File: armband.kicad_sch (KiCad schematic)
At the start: 14 parts, among them IC1 QSMP-1570, SW1 SW_MEC_5G, SW2 SW_MEC_5G

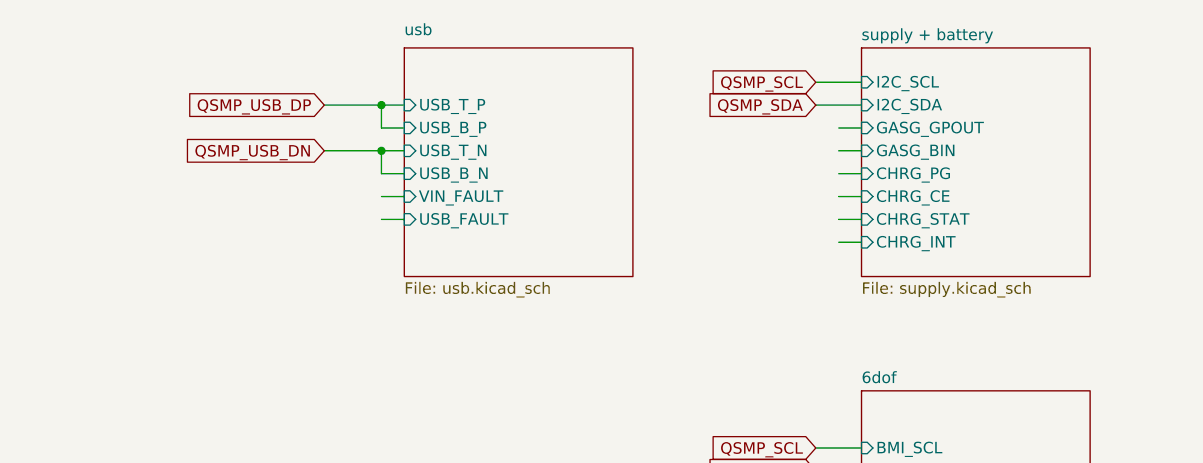
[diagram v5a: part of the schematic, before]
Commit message: switched to other charge + protection IC
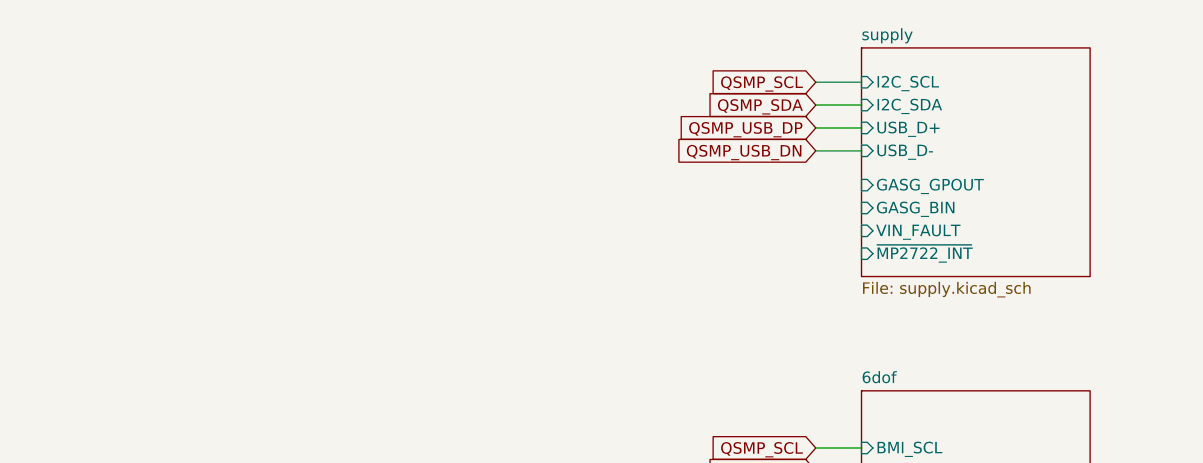
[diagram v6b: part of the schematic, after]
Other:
- sheet supply + battery renamed supply
- removed sheet usb
- sheet supply ports: added USB_D+, USB_D-, VIN_FAULT, ~{MP2722_INT}; removed CHRG_CE, CHRG_INT, CHRG_PG, CHRG_STAT
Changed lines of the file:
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@@
   (junction (at 44.45 99.06) (diameter 0) (color 0 0 0 0)
   )
-  (junction (at 314.96 31.75) (diameter 0) (color 0 0 0 0)
-  )
   (junction (at 35.56 40.64) (diameter 0) (color 0 0 0 0)
   )
@@
   (junction (at 190.5 248.92) (diameter 0) (color 0 0 0 0)
   )
-  (junction (at 314.96 36.83) (diameter 0) (color 0 0 0 0)
-  )
   (junction (at 185.42 55.88) (diameter 0) (color 0 0 0 0)
   )
@@
     (stroke (width 0) (type default))
   )
-  (wire (pts (xy 317.5 39.37) (xy 314.96 39.37))
-    (stroke (width 0) (type default))
-  )
-  (wire (pts (xy 365.76 41.91) (xy 368.3 41.91))
+  (wire (pts (xy 363.22 36.83) (xy 368.3 36.83))
     (stroke (width 0) (type default))
   )
@@
     (stroke (width 0) (type default))
   )
-  (wire (pts (xy 308.61 31.75) (xy 314.96 31.75))
-    (stroke (width 0) (type default))
-  )
   (polyline (pts (xy 25.4 121.92) (xy 25.4 76.2))
     (stroke (width 0) (type default))
@@
     (stroke (width 0) (type default))
   )
-  (wire (pts (xy 314.96 36.83) (xy 317.5 36.83))
-    (stroke (width 0) (type default))
-  )
   (wire (pts (xy 363.22 29.21) (xy 368.3 29.21))
     (stroke (width 0) (type default))
@@
     (stroke (width 0) (type default))
   )
-  (wire (pts (xy 365.76 34.29) (xy 368.3 34.29))
-    (stroke (width 0) (type default))
-  )
   (wire (pts (xy 233.68 213.36) (xy 236.22 213.36))
     (stroke (width 0) (type default))
@@
     (stroke (width 0) (type default))
   )
-  (wire (pts (xy 317.5 34.29) (xy 314.96 34.29))
-    (stroke (width 0) (type default))
-  )
   (wire (pts (xy 48.26 40.64) (xy 53.34 40.64))
     (stroke (width 0) (type default))
   )
-  (wire (pts (xy 308.61 36.83) (xy 314.96 36.83))
-    (stroke (width 0) (type default))
-  )
   (wire (pts (xy 33.02 257.81) (xy 38.1 257.81))
     (stroke (width 0) (type default))
@@
     (stroke (width 0) (type default))
   )
+  (wire (pts (xy 363.22 34.29) (xy 368.3 34.29))
+    (stroke (width 0) (type default))
+  )
   (wire (pts (xy 81.28 93.98) (xy 81.28 96.52))
     (stroke (width 0) (type default))
@@
     (stroke (width 0) (type default))
   )
-  (wire (pts (xy 314.96 36.83) (xy 314.96 39.37))
-    (stroke (width 0) (type default))
-  )
-  (wire (pts (xy 365.76 39.37) (xy 368.3 39.37))
-    (stroke (width 0) (type default))
-  )
   (polyline (pts (xy 25.4 76.2) (xy 101.6 76.2))
     (stroke (width 0) (type default))
@@
     (stroke (width 0) (type default))
   )
-  (wire (pts (xy 314.96 41.91) (xy 317.5 41.91))
-    (stroke (width 0) (type default))
-  )
   (wire (pts (xy 363.22 190.5) (xy 368.3 190.5))
     (stroke (width 0) (type default))
@@
     (stroke (width 0) (type default))
   )
-  (wire (pts (xy 314.96 31.75) (xy 317.5 31.75))
-    (stroke (width 0) (type default))
-  )
   (wire (pts (xy 81.28 257.81) (xy 83.82 257.81))
     (stroke (width 0) (type default))
@@
     (stroke (width 0) (type default))
   )
-  (wire (pts (xy 365.76 36.83) (xy 368.3 36.83))
-    (stroke (width 0) (type default))
-  )
   (wire (pts (xy 41.91 99.06) (xy 44.45 99.06))
     (stroke (width 0) (type default))
@@
     (stroke (width 0) (type default))
   )
-  (wire (pts (xy 314.96 44.45) (xy 317.5 44.45))
-    (stroke (width 0) (type default))
-  )
   (wire (pts (xy 185.42 55.88) (xy 187.96 55.88))
     (stroke (width 0) (type default))
@@
     (stroke (width 0) (type default))
   )
-  (wire (pts (xy 314.96 31.75) (xy 314.96 34.29))
-    (stroke (width 0) (type default))
-  )
   (wire (pts (xy 190.5 50.8) (xy 190.5 53.34))
     (stroke (width 0) (type default))
@@
     (stroke (width 0) (type default))
   )
-  (wire (pts (xy 365.76 46.99) (xy 368.3 46.99))
-    (stroke (width 0) (type default))
-  )
   (wire (pts (xy 81.28 96.52) (xy 83.82 96.52))
     (stroke (width 0) (type default))
@@
   )
   (wire (pts (xy 81.28 86.36) (xy 81.28 88.9))
-    (stroke (width 0) (type default))
-  )
-  (wire (pts (xy 365.76 44.45) (xy 368.3 44.45))
     (stroke (width 0) (type default))
   )
@@
     )
   )
-  (global_label "QSMP_USB_DN" (shape input) (at 308.61 36.83 180) (fields_autoplaced)
-    (effects (font (size 1.27 1.27)) (justify right))
-    (property "Intersheetrefs" "${INTERSHEET_REFS}" (at 292.0971 36.83 0)
+  (global_label "QSMP_USB_DN" (shape input) (at 363.22 36.83 180) (fields_autoplaced)
+    (effects (font (size 1.27 1.27)) (justify right))
+    (property "Intersheetrefs" "${INTERSHEET_REFS}" (at 346.7071 36.83 0)
       (effects (font (size 1.27 1.27)) (justify right) hide)
     )
@@
     )
   )
-  (global_label "QSMP_USB_DP" (shape input) (at 308.61 31.75 180) (fields_autoplaced)
-    (effects (font (size 1.27 1.27)) (justify right))
-    (property "Intersheetrefs" "${INTERSHEET_REFS}" (at 292.1576 31.75 0)
+  (global_label "QSMP_USB_DP" (shape input) (at 363.22 34.29 180) (fields_autoplaced)
+    (effects (font (size 1.27 1.27)) (justify right))
+    (property "Intersheetrefs" "${INTERSHEET_REFS}" (at 346.7676 34.29 0)
       (effects (font (size 1.27 1.27)) (justify right) hide)
     )
@@
         (path "/017c50c6-333c-4d31-ad5a-278994a09b14/ae5dc462-dca9-40e4-ba02-6b87a86a4904"
           (reference "C14") (unit 1)
-        )
-        (path "/017c50c6-333c-4d31-ad5a-278994a09b14/1029a9a3-b5d0-4240-805b-4fc2e9ca6858"
-          (reference "C19") (unit 1)
         )
       )
@@
         (path "/017c50c6-333c-4d31-ad5a-278994a09b14/ae5dc462-dca9-40e4-ba02-6b87a86a4904"
           (reference "C14") (unit 1)
-        )
-        (path "/017c50c6-333c-4d31-ad5a-278994a09b14/1029a9a3-b5d0-4240-805b-4fc2e9ca6858"
-          (reference "C19") (unit 1)
         )
       )
@@
           (reference "#PWR028") (unit 1)
         )
-        (path "/017c50c6-333c-4d31-ad5a-278994a09b14/1029a9a3-b5d0-4240-805b-4fc2e9ca6858"
-          (reference "#PWR011") (unit 1)
-        )
       )
     )
@@
           (reference "#PWR022") (unit 1)
         )
-        (path "/017c50c6-333c-4d31-ad5a-278994a09b14/1029a9a3-b5d0-4240-805b-4fc2e9ca6858"
-          (reference "#PWR010") (unit 1)
-        )
       )
     )
@@
         (path "/017c50c6-333c-4d31-ad5a-278994a09b14/ae5dc462-dca9-40e4-ba02-6b87a86a4904"
           (reference "C10") (unit 1)
-        )
-        (path "/017c50c6-333c-4d31-ad5a-278994a09b14/1029a9a3-b5d0-4240-805b-4fc2e9ca6858"
-          (reference "C20") (unit 1)
         )
       )
@@
         (path "/017c50c6-333c-4d31-ad5a-278994a09b14/ae5dc462-dca9-40e4-ba02-6b87a86a4904"
           (reference "C10") (unit 1)
-        )
-        (path "/017c50c6-333c-4d31-ad5a-278994a09b14/1029a9a3-b5d0-4240-805b-4fc2e9ca6858"
-          (reference "C20") (unit 1)
         )
       )
@@
     )
   )
-  (sheet (at 317.5 25.4) (size 25.4 25.4)
-    (stroke (width 0.1524) (type solid))
-    (fill (color 0 0 0 0.0000))
-    (property "Sheetname" "usb" (at 317.5 24.13 0)
-      (effects (font (size 1.27 1.27)) (justify left bottom))
-    )
-    (property "Sheetfile" "usb.kicad_sch" (at 317.5 51.3846 0)
-      (effects (font (size 1.27 1.27)) (justify left top))
-    )
-    (pin "VIN_FAULT" input (at 317.5 41.91 180)
-      (effects (font (size 1.27 1.27)) (justify left))
-    )
-    (pin "USB_T_N" input (at 317.5 36.83 180)
-      (effects (font (size 1.27 1.27)) (justify left))
-    )
-    (pin "USB_T_P" input (at 317.5 31.75 180)
-      (effects (font (size 1.27 1.27)) (justify left))
-    )
-    (pin "USB_B_P" input (at 317.5 34.29 180)
-      (effects (font (size 1.27 1.27)) (justify left))
-    )
-    (pin "USB_B_N" input (at 317.5 39.37 180)
-      (effects (font (size 1.27 1.27)) (justify left))
-    )
-    (pin "USB_FAULT" input (at 317.5 44.45 180)
-      (effects (font (size 1.27 1.27)) (justify left))
-    )
-    (instances
-      (project "armband"
-        (path "/017c50c6-333c-4d31-ad5a-278994a09b14" (page "8"))
-      )
-    )
-  )
   (sheet (at 368.3 63.5) (size 25.4 25.4) (fields_autoplaced)
     (stroke (width 0.1524) (type solid))
@@
     (stroke (width 0.1524) (type solid))
     (fill (color 0 0 0 0.0000))
-    (property "Sheetname" "supply + battery" (at 368.3 24.6884 0)
+    (property "Sheetname" "supply" (at 368.3 24.6884 0)
       (effects (font (size 1.27 1.27)) (justify left bottom))
     )
@@
       (effects (font (size 1.27 1.27)) (justify left))
     )
-    (pin "GASG_GPOUT" input (at 368.3 34.29 180)
-      (effects (font (size 1.27 1.27)) (justify left))
-    )
-    (pin "GASG_BIN" input (at 368.3 36.83 180)
-      (effects (font (size 1.27 1.27)) (justify left))
-    )
-    (pin "CHRG_PG" input (at 368.3 39.37 180)
-      (effects (font (size 1.27 1.27)) (justify left))
-    )
-    (pin "CHRG_CE" input (at 368.3 41.91 180)
-      (effects (font (size 1.27 1.27)) (justify left))
-    )
-    (pin "CHRG_STAT" input (at 368.3 44.45 180)
-      (effects (font (size 1.27 1.27)) (justify left))
-    )
-    (pin "CHRG_INT" input (at 368.3 46.99 180)
-      (effects (font (size 1.27 1.27)) (justify left))
-    )
+    (pin "GASG_GPOUT" input (at 368.3 40.64 180)
+      (effects (font (size 1.27 1.27)) (justify left))
+    )
+    (pin "GASG_BIN" input (at 368.3 43.18 180)
+      (effects (font (size 1.27 1.27)) (justify left))
+    )
+    (pin "USB_D-" input (at 368.3 36.83 180)
+      (effects (font (size 1.27 1.27)) (justify left))
+    )
+    (pin "USB_D+" input (at 368.3 34.29 180)
+      (effects (font (size 1.27 1.27)) (justify left))
+    )
+    (pin "VIN_FAULT" input (at 368.3 45.72 180)
+      (effects (font (size 1.27 1.27)) (justify left))
+    )
+    (pin "~{MP2722_INT}" input (at 368.3 48.26 180)
+      (effects (font (size 1.27 1.27)) (justify left))
+    )

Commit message: Add i2c device list
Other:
- note added: "I²C Device List | Name | Addr | Alt | |---------------|------|------| |Battery Charge | 0x3F | | |Gauge | 0x55 | | |6dof | 0x68 | 0x69 | |Heart Rate | 0xAE | | |Touch | 0x24 | | |BLE + NFC | prog. |"
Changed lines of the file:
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@@
     (effects (font (size 1.27 1.27)) (justify left bottom))
+  )
+  (text "I²C Device List\n\n| Name          | Addr | Alt  |\n|---------------|------|------|\n|Battery Charge | 0x3F |      |	\n|Gauge          | 0x55 |      |	\n|6dof           | 0x68 | 0x69 |\n|Heart Rate     | 0xAE |      |\n|Touch          | 0x24 |      |\n|BLE + NFC      | prog.       |\n"
+    (at 304.8 38.1 0)
+    (effects (font (face "Cascadia Mono") (size 1.27 1.27)) (justify left bottom))
   )
   (text "H=Flash boot\nL=USB/UART" (at 45.72 90.17 0)

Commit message: added decoupling capacitors to sensors
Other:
- note removed: "I²C Device List | Name | Addr | Alt | |---------------|------|------| |Battery Charge | 0x3F | | |Gauge | 0x55 | | |6dof | 0x68 | 0x69 | |Heart Rate | 0xAE | | |Touch | 0x24 | | |BLE + NFC | prog. |"
- moved on the sheet: C2
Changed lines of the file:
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@@
     (stroke (width 0) (type default))
   )
-  (wire (pts (xy 81.28 101.6) (xy 81.28 96.52))
+  (wire (pts (xy 81.28 99.06) (xy 81.28 96.52))
     (stroke (width 0) (type default))
   )
@@
   )
   (polyline (pts (xy 101.6 76.2) (xy 101.6 121.92))
+    (stroke (width 0) (type default))
+  )
+  (wire (pts (xy 81.28 104.14) (xy 81.28 106.68))
     (stroke (width 0) (type default))
   )
@@
   (text "Supply" (at 26.67 27.94 0)
     (effects (font (size 1.27 1.27)) (justify left bottom))
-  )
-  (text "I²C Device List\n\n| Name          | Addr | Alt  |\n|---------------|------|------|\n|Battery Charge | 0x3F |      |	\n|Gauge          | 0x55 |      |	\n|6dof           | 0x68 | 0x69 |\n|Heart Rate     | 0xAE |      |\n|Touch          | 0x24 |      |\n|BLE + NFC      | prog.       |\n"
-    (at 304.8 38.1 0)
-    (effects (font (face "Cascadia Mono") (size 1.27 1.27)) (justify left bottom))
   )
   (text "H=Flash boot\nL=USB/UART" (at 45.72 90.17 0)
@@
     )
   )
-  (symbol (lib_id "Device:C_Small") (at 81.28 104.14 0) (unit 1)
+  (symbol (lib_id "Device:C_Small") (at 81.28 101.6 0) (unit 1)
     (in_bom yes) (on_board yes) (dnp no) (fields_autoplaced)
-    (property "Reference" "C2" (at 83.82 103.5113 0)
+    (property "Reference" "C2" (at 83.82 100.9713 0)
       (effects (font (size 1.27 1.27)) (justify left))
     )
-    (property "Value" "10n" (at 83.82 106.0513 0)
+    (property "Value" "10n" (at 83.82 103.5113 0)
       (effects (font (size 1.27 1.27)) (justify left))
     )
-    (property "Footprint" "Capacitor_SMD:C_0402_1005Metric" (at 81.28 104.14 0)
-      (effects (font (size 1.27 1.27)) hide)
-    )
-    (property "Datasheet" "~" (at 81.28 104.14 0)
-      (effects (font (size 1.27 1.27)) hide)
-    )
-    (property "MFN" " 77-VJ0603Y103MXAPBC " (at 81.28 104.14 0)
-      (effects (font (size 1.27 1.27)) hide)
-    )
+    (property "Footprint" "Capacitor_SMD:C_0402_1005Metric" (at 81.28 101.6 0)
+      (effects (font (size 1.27 1.27)) hide)
+    )
+    (property "Datasheet" "~" (at 81.28 101.6 0)
+      (effects (font (size 1.27 1.27)) hide)
+    )
+    (property "MFN" " 77-VJ0603Y103MXAPBC " (at 81.28 101.6 0)
+      (effects (font (size 1.27 1.27)) hide)
+    )
